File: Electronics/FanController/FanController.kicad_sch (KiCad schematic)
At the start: 26 parts, among them Q1 IRLZ44N, SW1 RST_BUTTON, U1 STM32L051K8Tx, Y1 Crystal

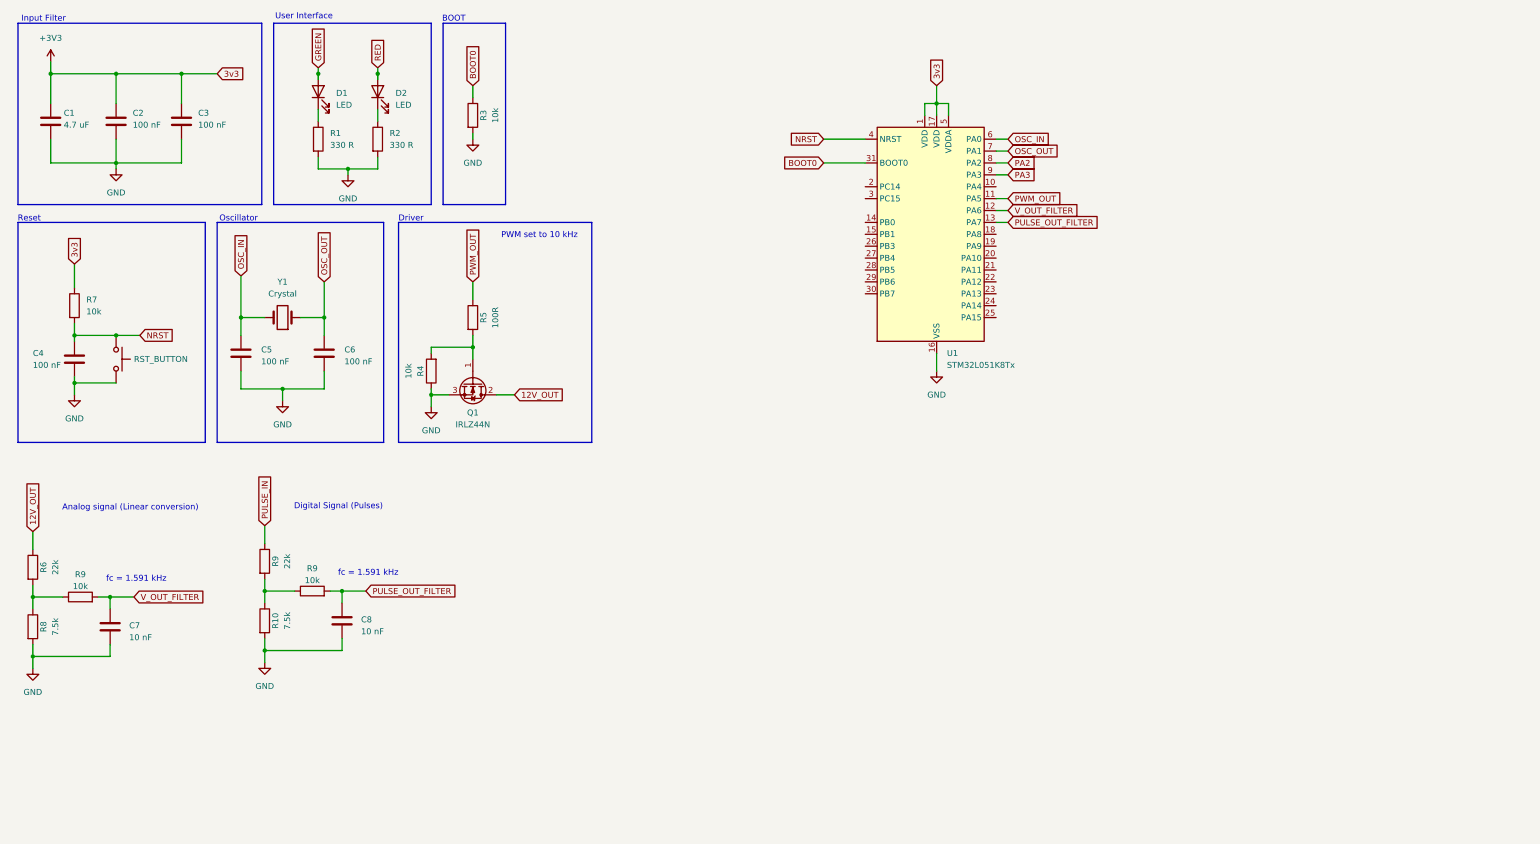
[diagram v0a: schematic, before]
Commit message: Added headers
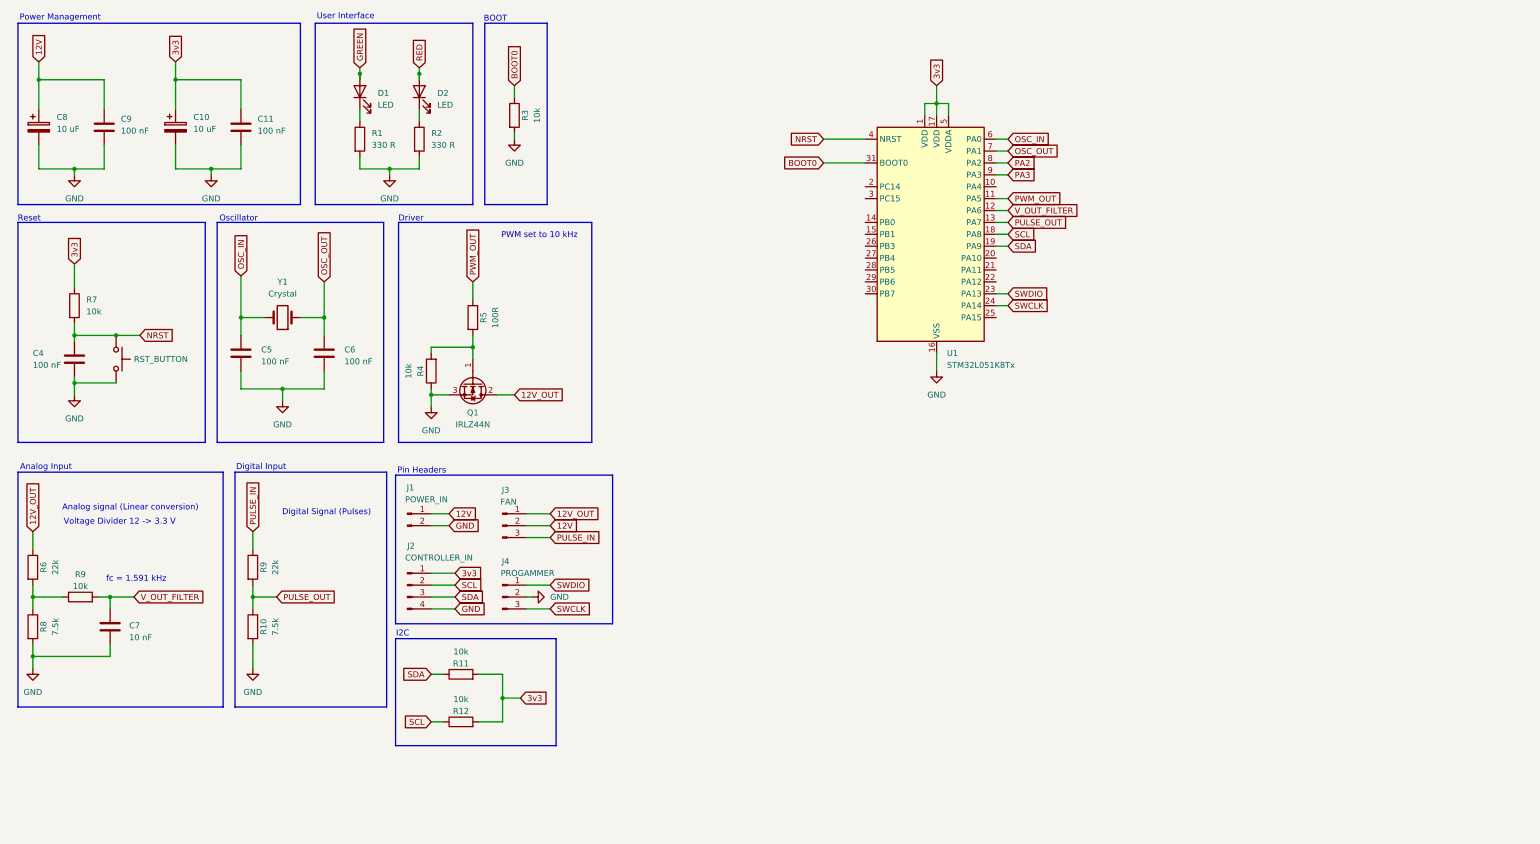
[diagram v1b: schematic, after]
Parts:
- removed 10k: R9, symbol Device:R
- removed C1: 4.7 uF, symbol Device:C
- removed C2, C3: 100 nF, symbol Device:C
- removed C8: 10 nF, symbol Device:C
- added C10, C8: 10 uF, symbol Device:C_Polarized
- added C11, C9: 100 nF, symbol Device:C
- added J1: POWER_IN, symbol Connector:Conn_01x02_Pin
- added J2: CONTROLLER_IN, symbol Connector:Conn_01x04_Pin
- added J3: FAN, symbol Connector:Conn_01x03_Pin
- added J4: PROGAMMER, symbol Connector:Conn_01x03_Pin
- added R11, R12: 10k, symbol Device:R
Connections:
- net PULSE_OUT_FILTER is gone; now on net PULSE_OUT: U1.13 (PA7)
- net 12V_OUT: now also J3.1 (Pin_1)
- net GND: now also C10.2, C11.2, C8.2, C9.2, J1.2 (Pin_2), J2.4 (Pin_4), J4.2 (Pin_2)
- net PULSE_IN: now also J3.3 (Pin_3)
- net PULSE_OUT: now reaches R10.1, R9.2
- net SCL: now reaches U1.18 (PA8)
- net SCL: now also J2.2 (Pin_2), R12.1
- net SDA: now reaches U1.19 (PA9)
- net SDA: now also J2.3 (Pin_3), R11.1
- net SWDIO: now reaches U1.23 (PA13)
- net SWDIO: now also J4.1 (Pin_1)
- net SWCLK: now reaches U1.24 (PA14)
- net SWCLK: now also J4.3 (Pin_3)
- net +3V3 renamed 3v3
- net 3v3: now also C10.1, C11.1, J2.1 (Pin_1), R11.2, R12.2
- new net 12V: C8.1, C9.1, J1.1 (Pin_1), J3.2 (Pin_2)
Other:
- note added: "Analog Input"
- note added: "Digital Input"
- note added: "I2C"
- note added: "Pin Headers"
- note added: "Power Management"
- note added: "Voltage Divider 12 -> 3.3 V"
- note removed: "Input Filter"
- moved on the sheet: D1, D2, R1, R10, R2, R3, R9

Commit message: Added current measurement and reverse polarity protection
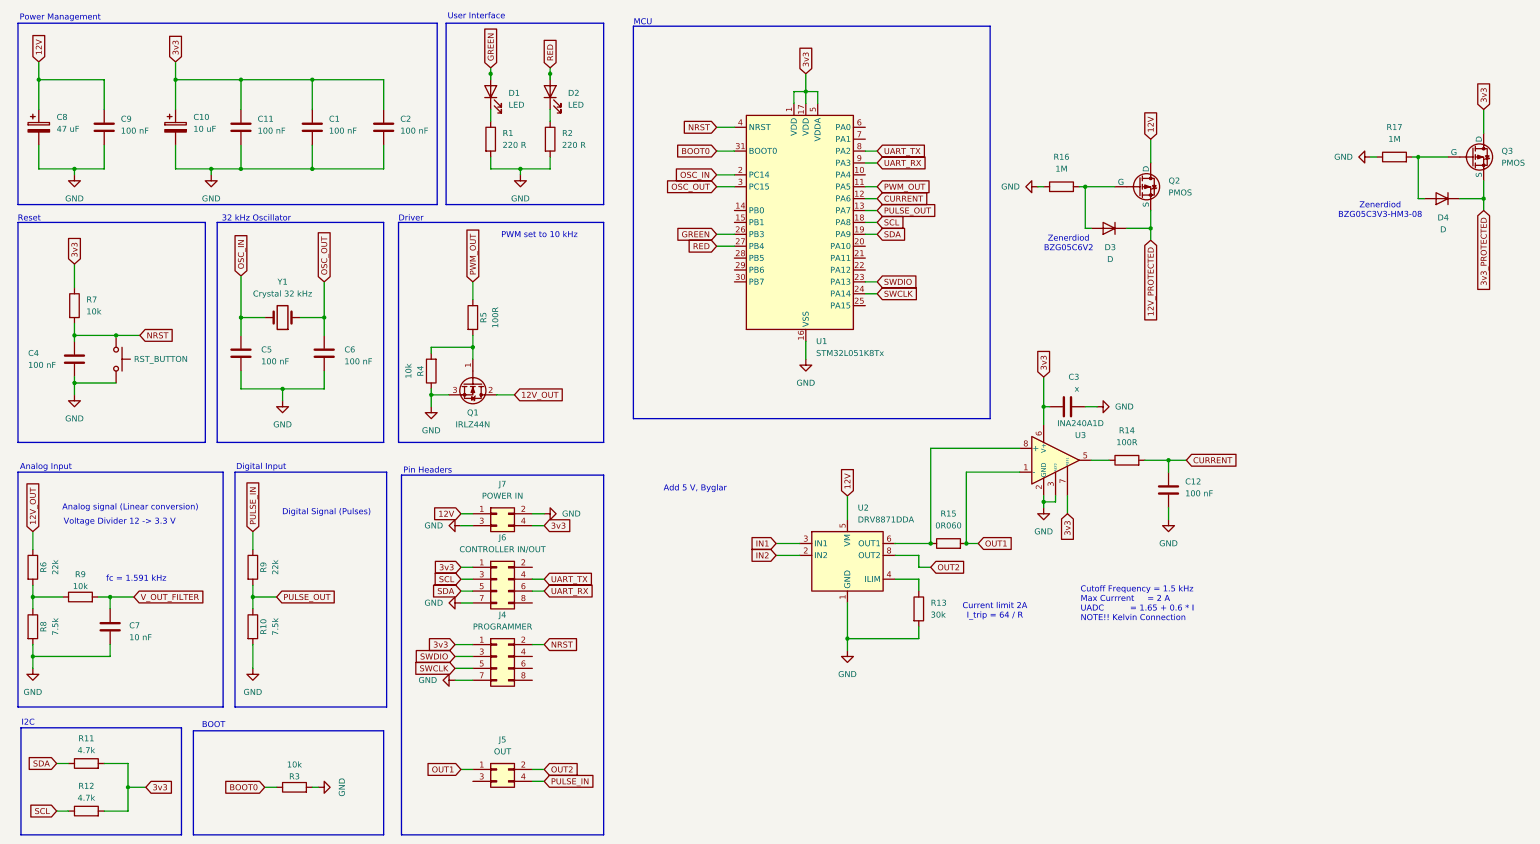
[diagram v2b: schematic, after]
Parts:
- removed J1: POWER_IN, symbol Connector:Conn_01x02_Pin
- removed J2: CONTROLLER_IN, symbol Connector:Conn_01x04_Pin
- removed J3: FAN, symbol Connector:Conn_01x03_Pin
- removed J4: PROGAMMER, symbol Connector:Conn_01x03_Pin
- added C1, C12, C2: 100 nF, symbol Device:C
- added C3: x, symbol Device:C
- added D3, D4: D, symbol Device:D
- added J4: PROGRAMMER, symbol Connector_Generic:Conn_02x04_Odd_Even
- added J5: OUT, symbol Connector_Generic:Conn_02x02_Odd_Even
- added J6: CONTROLLER IN/OUT, symbol Connector_Generic:Conn_02x04_Odd_Even
- added J7: POWER IN, symbol Connector_Generic:Conn_02x02_Odd_Even
- added Q2, Q3: PMOS, symbol Simulation_SPICE:PMOS
- added R13: 30k, symbol Device:R
- added R14: 100R, symbol Device:R
- added R15: 0R060, symbol Device:R
- added R16, R17: 1M, symbol Device:R
- added U2: DRV8871DDA, Package_SO:Texas_HTSOP-8-1EP_3.9x4.9mm_P1.27mm_EP2.95x4.9mm_Mask2.4x3.1mm_ThermalVias, symbol Driver_Motor:DRV8871DDA
- added U3: INA240A1D, Package_SO:SOIC-8_3.9x4.9mm_P1.27mm, symbol Amplifier_Current:INA240A1D
- C8: value 10 uF -> 47 uF
- R1, R2: value 330 R -> 220 R
- R11, R12: value 10k -> 4.7k
- Y1: value Crystal -> Crystal 32 kHz
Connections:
- net 12V: now also J7.1 (Pin_1), Q2.1 (D), U2.5 (VM)
- net 3v3: now also C1.1, C2.1, C3.1, J4.1 (Pin_1), J6.1 (Pin_1), J7.4 (Pin_4), Q3.1 (D), U3.6 (V+), U3.7 (REF1)
- net GND: now also C1.2, C12.2, C2.2, C3.2, J4.7 (Pin_7), J6.7 (Pin_7), J7.2 (Pin_2), J7.3 (Pin_3), R13.2, R16.1, R17.1, U2.1 (GND), U2.7 (GND), U2.9 (GND), U3.2 (GND), U3.3 (REF2), U3.4 (GND)
- net GREEN: now also U1.26 (PB3)
- net NRST: now also J4.2 (Pin_2)
- net OSC_IN: now also U1.2 (PC14); no longer U1.6 (PA0)
- net OSC_OUT: now also U1.3 (PC15); no longer U1.7 (PA1)
- net PULSE_IN: now also J5.4 (Pin_4)
- net RED: now also U1.27 (PB4)
- net SCL: now also J6.3 (Pin_3)
- net SDA: now also J6.5 (Pin_5)
- net SWCLK: now also J4.5 (Pin_5)
- net SWDIO: now also J4.3 (Pin_3)
- net V_OUT_FILTER: no longer U1.12 (PA6)
- net PA2 renamed UART_TX
- net UART_TX: now also J6.4 (Pin_4)
- net PA3 renamed UART_RX
- net UART_RX: now also J6.6 (Pin_6)
- new net: R14.1, U3.5
- new net: D4.2 (A), Q3.2 (G), R17.2
- new net: R15.1, U2.6 (OUT1), U3.8 (+)
- new net: D3.2 (A), Q2.2 (G), R16.2
- new net: R13.1, U2.4 (ILIM)
- new net 12V_PROTECTED: D3.1 (K), Q2.3 (S)
- new net 3v3_PROTECTED: D4.1 (K), Q3.3 (S)
- new net CURRENT: C12.1, R14.2, U1.12 (PA6)
- new net IN1: U2.3 (IN1)
- new net IN2: U2.2 (IN2)
- new net OUT1: J5.1 (Pin_1), R15.2, U3.1 (-)
- new net OUT2: J5.2 (Pin_2), U2.8 (OUT2)
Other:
- note added: "32 kHz Oscillator"
- note added: "Add 5 V, Byglar"
- note added: "Current limit 2A I_trip = 64 / R"
- note added: "Cutoff Frequency = 1.5 kHz Max Currrent = 2 A UADC = 1.65 + 0.6 * I NOTE!! Kelvin Connection"
- note added: "MCU"
- note added: "Zenerdiod BZG05C3V3-HM3-08"
- note added: "Zenerdiod BZG05C6V2"
- note removed: "Oscillator"
- moved on the sheet: D1, D2, R1, R11, R12, R2, R3, U1
